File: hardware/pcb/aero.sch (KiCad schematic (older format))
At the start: 0 parts

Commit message: version 1 of layout
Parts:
- added H1: Vreg_Header, Socket_Strips:Socket_Strip_Straight_1x02, symbol Vreg_Header
- added P1: CONN_01X09, Socket_Strips:Socket_Strip_Straight_1x09, symbol CONN_01X09
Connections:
- net nRF8001/ACTIVE: now also P1.9 (P9)
- net nRF8001/MISO: now also P1.3 (P3)
- net nRF8001/MOSI: now also P1.4 (P4)
- net nRF8001/SCK: now also P1.6 (P6)
- net nRF8001/TXD: now also P1.8 (P8)
- net nRF8001/~RDYN: now also P1.2 (P2)
- net nRF8001/~REQN: now also P1.5 (P5)
- net nRF8001/~RESET: now also P1.1 (P1)
- new net nRF8001/Gnd: H1.2 (GND)
- new net nRF8001/RXD: P1.7 (P7)
- new net nRF8001/Vcc: H1.1 (Vcc)
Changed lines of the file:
@@
 LIBS:contrib
 LIBS:valves
+LIBS:aero-cache
 EELAYER 25 0
 EELAYER END
@@
 Comment4 ""
 $EndDescr
+$Comp
+L CONN_01X09 P1
+U 1 1 551C5BBD
+P 7550 1650
+F 0 "P1" H 7550 2150 50  0000 C CNN
+F 1 "CONN_01X09" V 7650 1650 50  0000 C CNN
+F 2 "Socket_Strips:Socket_Strip_Straight_1x09" H 7550 1650 60  0001 C CNN
+F 3 "" H 7550 1650 60  0000 C CNN
+	1    7550 1650
+	-1   0    0    1
+$EndComp
+$Comp
+L Vreg_Header H1
+U 1 1 551C5F7E
+P 7550 2450
+F 0 "H1" H 7500 2400 60  0000 C CNN
+F 1 "Vreg_Header" V 7350 2400 60  0000 C CNN
+F 2 "Socket_Strips:Socket_Strip_Straight_1x02" H 7550 2450 60  0001 C CNN
+F 3 "" H 7550 2450 60  0000 C CNN
+	1    7550 2450
+	1    0    0    -1
+$EndComp
+Wire Wire Line
+	7800 2300 8000 2300
+Wire Wire Line
+	8000 2400 7800 2400
 $Sheet
 S 8000 1150 1950 1350
@@
 F0 "nRF8001" 60
 F1 "nrf8001.sch" 60
-F2 "MOSI" I L 8000 1450 60
-F3 "MISO" O L 8000 1550 60
-F4 "~RDYN" O L 8000 1650 60
-F5 "~REQN" I L 8000 1750 60
-F6 "SCK" I L 8000 1350 60
-F7 "~RESET" I L 8000 1850 60
-F8 "ACTIVE" I L 8000 1950 60
-F9 "TXD" O L 8000 2050 60
+F2 "Vcc" I L 8000 2300 60
+F3 "Gnd" I L 8000 2400 60
+F4 "MOSI" I L 8000 1750 60
+F5 "MISO" O L 8000 1850 60
+F6 "~RDYN" O L 8000 1950 60
+F7 "~REQN" I L 8000 1650 60
+F8 "SCK" I L 8000 1550 60
+F9 "~RESET" I L 8000 2050 60
+F10 "ACTIVE" I L 8000 1250 60
+F11 "TXD" I L 8000 1350 60
+F12 "RXD" I L 8000 1450 60
 $EndSheet
+Wire Wire Line
+	7750 1250 8000 1250
+Wire Wire Line
+	8000 1350 7750 1350
+Wire Wire Line
+	7750 1450 8000 1450
+Wire Wire Line
+	8000 1550 7750 1550
+Wire Wire Line
+	8000 1650 7750 1650
+Wire Wire Line
+	7750 1750 8000 1750
+Wire Wire Line
+	8000 1850 7750 1850
+Wire Wire Line
+	7750 1950 8000 1950
+Wire Wire Line
+	8000 2050 7750 2050
 $EndSCHEMATC

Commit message: pcb updates
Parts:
- added P1: CONN_01X02, Pin_Headers:Pin_Header_Straight_1x02, symbol CONN_01X02
- H1: footprint Socket_Strips:Socket_Strip_Straight_1x02 -> Pin_Headers:Pin_Header_Straight_1x02
- P2: renamed from P1; footprint Socket_Strips:Socket_Strip_Straight_1x09 -> Pin_Headers:Pin_Header_Straight_1x09
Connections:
- net labels added: GND, VCC
- wire segments 11 -> 16
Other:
- moved on the sheet: H1
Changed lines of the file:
@@
 $Descr A4 11693 8268
 encoding utf-8
-Sheet 1 2
+Sheet 1 3
 Title ""
 Date ""
@@
 $EndDescr
 $Comp
-L CONN_01X09 P1
+L CONN_01X09 P2
 U 1 1 551C5BBD
 P 7550 1650
-F 0 "P1" H 7550 2150 50  0000 C CNN
+F 0 "P2" H 7550 2150 50  0000 C CNN
 F 1 "CONN_01X09" V 7650 1650 50  0000 C CNN
-F 2 "Socket_Strips:Socket_Strip_Straight_1x09" H 7550 1650 60  0001 C CNN
+F 2 "Pin_Headers:Pin_Header_Straight_1x09" H 7550 1650 60  0001 C CNN
 F 3 "" H 7550 1650 60  0000 C CNN
 	1    7550 1650
@@
 L Vreg_Header H1
 U 1 1 551C5F7E
-P 7550 2450
-F 0 "H1" H 7500 2400 60  0000 C CNN
-F 1 "Vreg_Header" V 7350 2400 60  0000 C CNN
-F 2 "Socket_Strips:Socket_Strip_Straight_1x02" H 7550 2450 60  0001 C CNN
-F 3 "" H 7550 2450 60  0000 C CNN
-	1    7550 2450
+P 6000 3250
+F 0 "H1" H 5950 3200 60  0000 C CNN
+F 1 "Vreg_Header" V 5800 3200 60  0000 C CNN
+F 2 "Pin_Headers:Pin_Header_Straight_1x02" H 6000 3250 60  0001 C CNN
+F 3 "" H 6000 3250 60  0000 C CNN
+	1    6000 3250
 	1    0    0    -1
 $EndComp
-Wire Wire Line
-	7800 2300 8000 2300
-Wire Wire Line
-	8000 2400 7800 2400
 $Sheet
 S 8000 1150 1950 1350
@@
 F0 "nRF8001" 60
 F1 "nrf8001.sch" 60
-F2 "Vcc" I L 8000 2300 60
-F3 "Gnd" I L 8000 2400 60
-F4 "MOSI" I L 8000 1750 60
-F5 "MISO" O L 8000 1850 60
-F6 "~RDYN" O L 8000 1950 60
-F7 "~REQN" I L 8000 1650 60
-F8 "SCK" I L 8000 1550 60
-F9 "~RESET" I L 8000 2050 60
-F10 "ACTIVE" I L 8000 1250 60
-F11 "TXD" I L 8000 1350 60
-F12 "RXD" I L 8000 1450 60
+F2 "MOSI" I L 8000 1750 60
+F3 "MISO" O L 8000 1850 60
+F4 "~RDYN" O L 8000 1950 60
+F5 "~REQN" I L 8000 1650 60
+F6 "SCK" I L 8000 1550 60
+F7 "~RESET" I L 8000 2050 60
+F8 "ACTIVE" I L 8000 1250 60
+F9 "TXD" I L 8000 1350 60
+F10 "RXD" I L 8000 1450 60
 $EndSheet
+$Sheet
+S 2800 1050 1400 1200
+U 551EEA41
+F0 "sensors" 60
+F1 "sensors.sch" 60
+F2 "SDA" I R 4200 1250 60
+F3 "SCLK" I R 4200 1400 60
+$EndSheet
+Text GLabel 6900 3050 2    60   Input ~ 0
+VCC
+Text GLabel 6900 3250 2    60   Input ~ 0
+GND
+$Comp
+L CONN_01X02 P1
+U 1 1 551EFD46
+P 4700 1300
+F 0 "P1" H 4700 1450 50  0000 C CNN
+F 1 "CONN_01X02" V 4800 1300 50  0000 C CNN
+F 2 "Pin_Headers:Pin_Header_Straight_1x02" H 4700 1300 60  0001 C CNN
+F 3 "" H 4700 1300 60  0000 C CNN
+	1    4700 1300
+	1    0    0    -1
+$EndComp
 Wire Wire Line
 	7750 1250 8000 1250
@@
 Wire Wire Line
 	8000 2050 7750 2050
+Wire Wire Line
+	6900 3250 6250 3250
+Wire Wire Line
+	6250 3250 6250 3200
+Wire Wire Line
+	6250 3100 6900 3100
+Wire Wire Line
+	6900 3100 6900 3050
+Wire Wire Line
+	4200 1250 4500 1250
+Wire Wire Line
+	4200 1400 4500 1400
+Wire Wire Line
+	4500 1400 4500 1350
 $EndSCHEMATC

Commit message: PCB updates, new docs, file reorg
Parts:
- removed P1: CONN_01X02, Pin_Headers:Pin_Header_Straight_1x02, symbol CONN_01X02
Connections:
- wire segments 16 -> 13
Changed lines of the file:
@@
 $Descr A4 11693 8268
 encoding utf-8
-Sheet 1 3
+Sheet 1 4
 Title ""
 Date ""
@@
 $EndSheet
 $Sheet
-S 2800 1050 1400 1200
+S 2800 1050 700  650
 U 551EEA41
-F0 "sensors" 60
-F1 "sensors.sch" 60
-F2 "SDA" I R 4200 1250 60
-F3 "SCLK" I R 4200 1400 60
+F0 "ms5611" 60
+F1 "ms5611.sch" 60
+F2 "EN" I R 3500 1350 60
+F3 "SCLK" I R 3500 1650 60
+F4 "MOSI" I R 3500 1450 60
+F5 "MISO" I R 3500 1550 60
 $EndSheet
 Text GLabel 6900 3050 2    60   Input ~ 0
@@
 Text GLabel 6900 3250 2    60   Input ~ 0
 GND
-$Comp
-L CONN_01X02 P1
-U 1 1 551EFD46
-P 4700 1300
-F 0 "P1" H 4700 1450 50  0000 C CNN
-F 1 "CONN_01X02" V 4800 1300 50  0000 C CNN
-F 2 "Pin_Headers:Pin_Header_Straight_1x02" H 4700 1300 60  0001 C CNN
-F 3 "" H 4700 1300 60  0000 C CNN
-	1    4700 1300
-	1    0    0    -1
-$EndComp
 Wire Wire Line
 	7750 1250 8000 1250
@@
 Wire Wire Line
 	6900 3100 6900 3050
-Wire Wire Line
-	4200 1250 4500 1250
-Wire Wire Line
-	4200 1400 4500 1400
-Wire Wire Line
-	4500 1400 4500 1350
+$Sheet
+S 2600 2450 650  500
+U 5527E8E0
+F0 "bmx055" 60
+F1 "bmx055.sch" 60
+$EndSheet
 $EndSCHEMATC

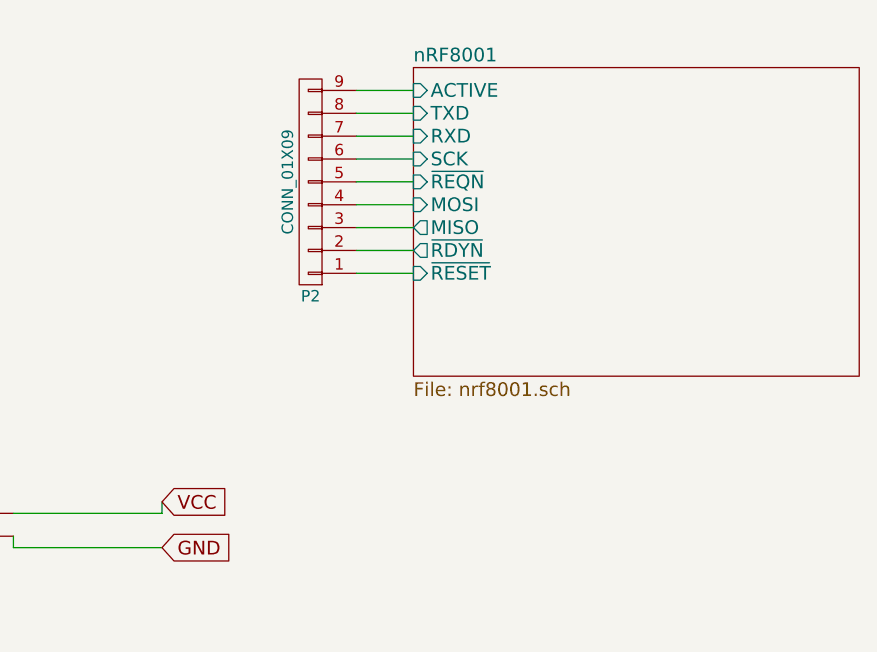
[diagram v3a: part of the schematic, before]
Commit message: Removed nRF8001 connections; beginning eventual design
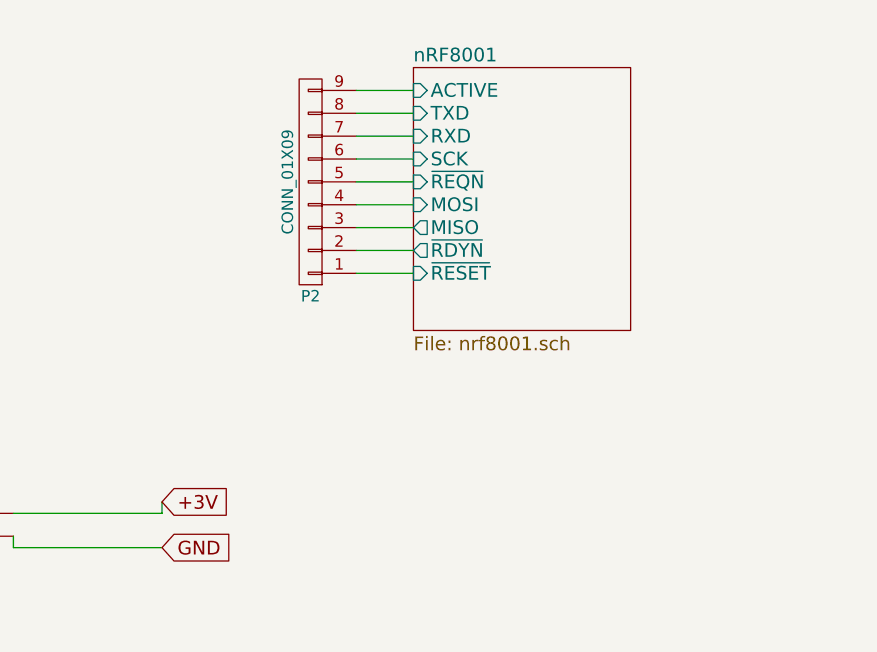
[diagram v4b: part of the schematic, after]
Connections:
- net VCC renamed +3V
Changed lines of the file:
@@
 $EndComp
 $Sheet
-S 8000 1150 1950 1350
+S 8000 1150 950  1150
 U 551C09E8
 F0 "nRF8001" 60
@@
 $EndSheet
 Text GLabel 6900 3050 2    60   Input ~ 0
-VCC
++3V
 Text GLabel 6900 3250 2    60   Input ~ 0
 GND

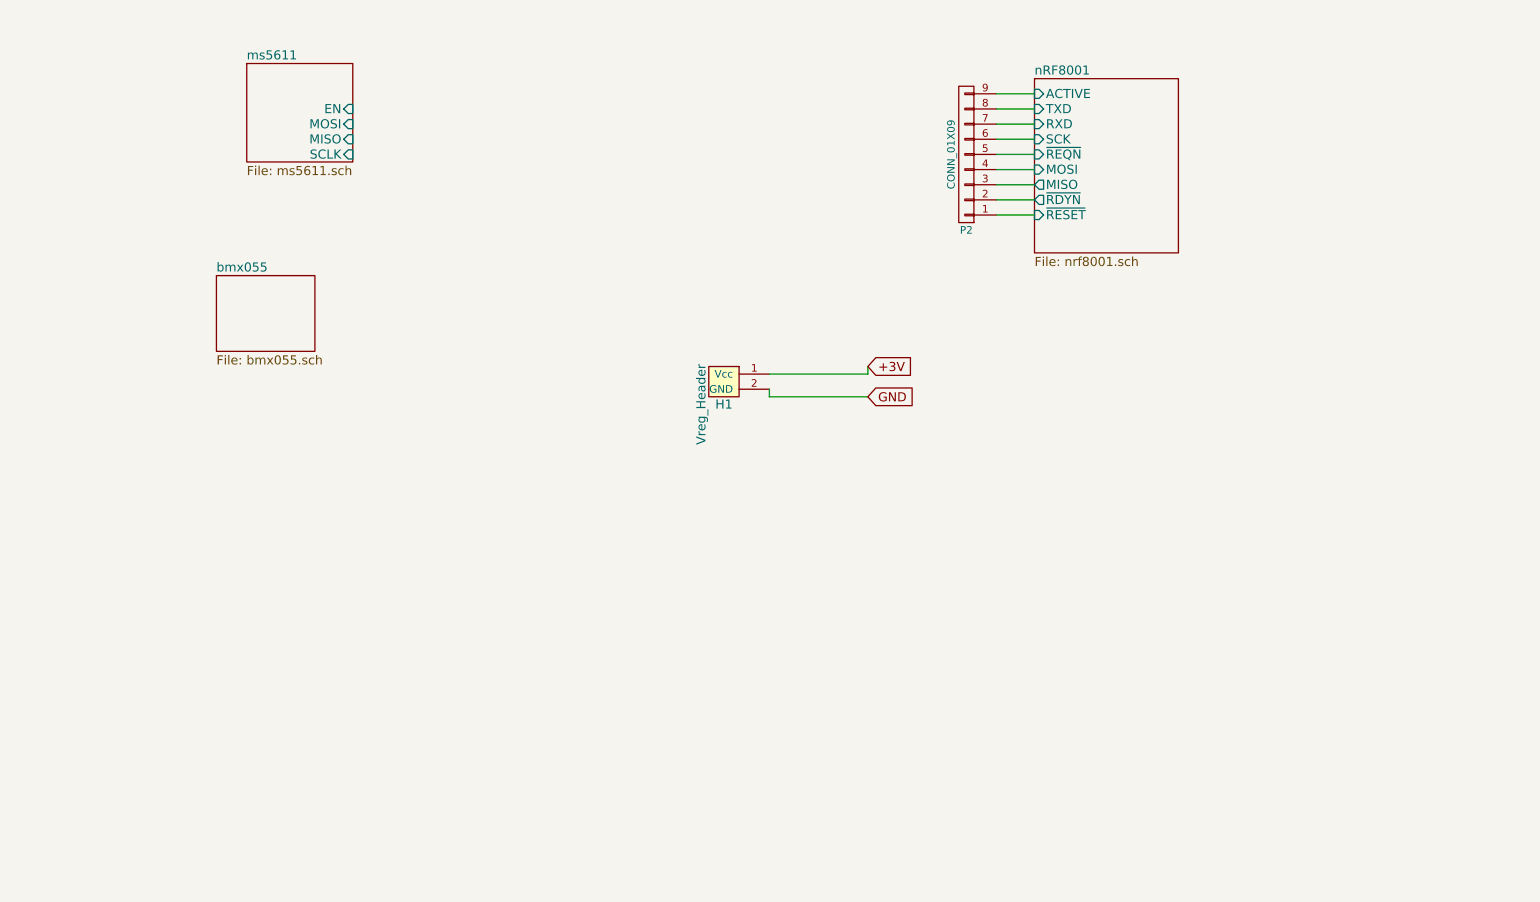
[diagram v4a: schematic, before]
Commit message: Added mcu, connected nrf8001 and flash, new footprint, other changes
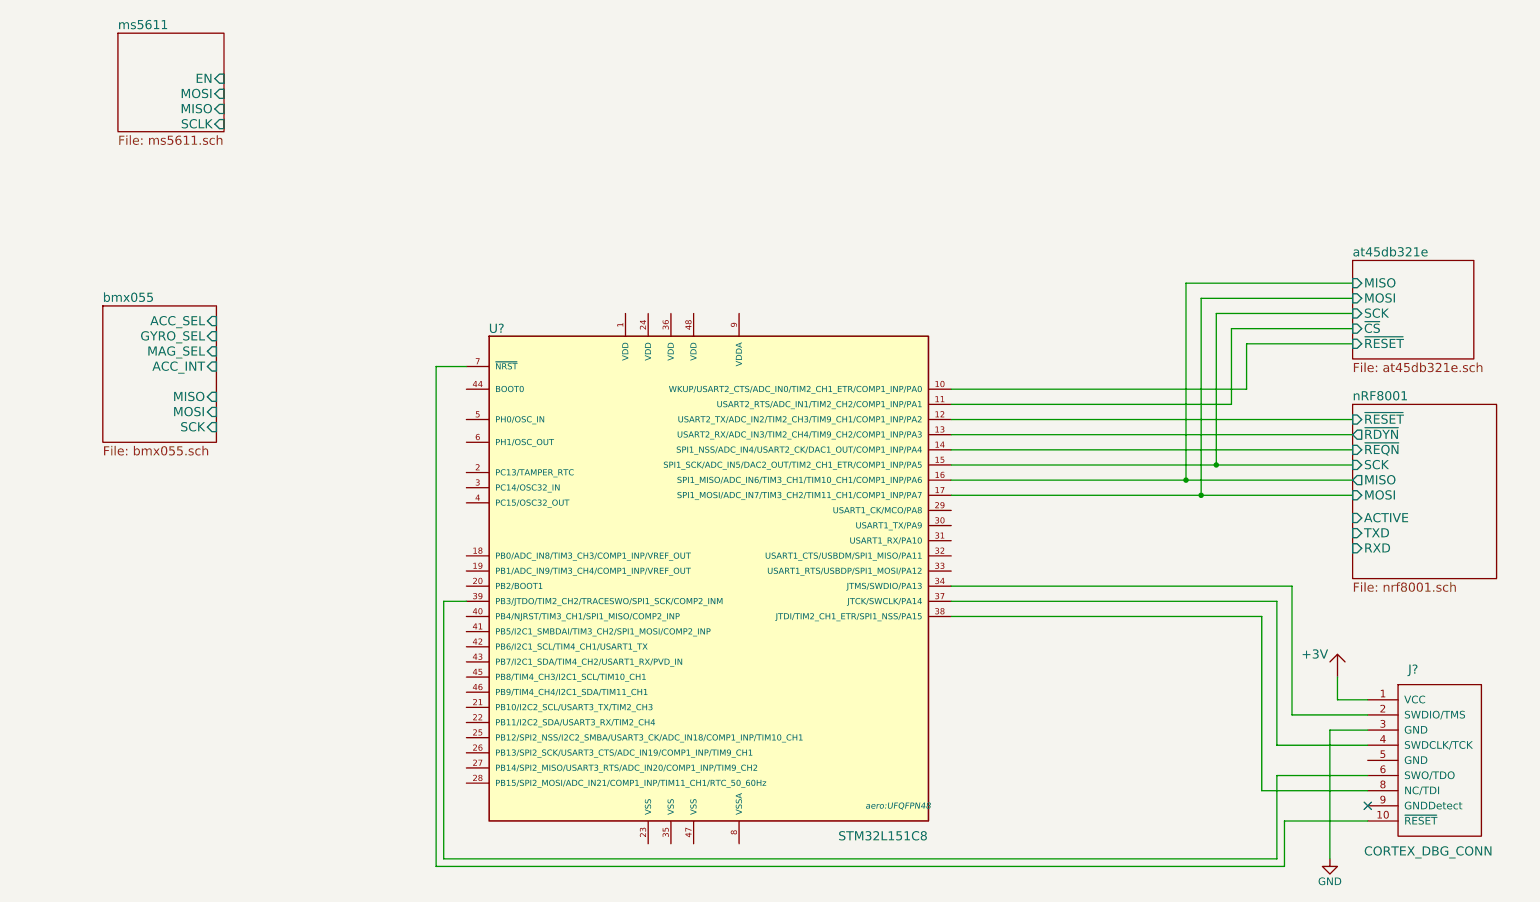
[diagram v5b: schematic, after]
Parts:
- removed H1: Vreg_Header, Pin_Headers:Pin_Header_Straight_1x02, symbol Vreg_Header
- removed P2: CONN_01X09, Pin_Headers:Pin_Header_Straight_1x09, symbol CONN_01X09
- added J?: CORTEX_DBG_CONN, symbol CORTEX_DBG_CONN
- added U?: STM32L151C8, aero:UFQFPN48, symbol STM32L151C8
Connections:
- net GND: now also J?.3 (GND)
- net nRF8001/~RDYN: now also U?.13 (USART2_RX/ADC_IN3/TIM2_CH4/TIM9_CH2/COMP1_INP/PA3)
- net nRF8001/~REQN: now also U?.14 (SPI1_NSS/ADC_IN4/USART2_CK/DAC1_OUT/COMP1_INP/PA4)
- net nRF8001/~RESET: now also U?.12 (USART2_TX/ADC_IN2/TIM2_CH3/TIM9_CH1/COMP1_INP/PA2)
- new net: J?.2 (SWDIO/TMS), U?.34 (JTMS/SWDIO/PA13)
- new net: J?.4 (SWDCLK/TCK), U?.37 (JTCK/SWCLK/PA14)
- new net: J?.8 (NC/TDI), U?.38 (JTDI/TIM2_CH1_ETR/SPI1_NSS/PA15)
- new net: J?.6 (SWO/TDO), U?.39 (PB3/JTDO/TIM2_CH2/TRACESWO/SPI1_SCK/COMP2_INM)
- new net: J?.10 (~RESET), U?.7 (~NRST)
- new net +3V3: J?.1 (VCC)
- new net at45db321e/MISO: U?.16 (SPI1_MISO/ADC_IN6/TIM3_CH1/TIM10_CH1/COMP1_INP/PA6)
- new net at45db321e/MOSI: U?.17 (SPI1_MOSI/ADC_IN7/TIM3_CH2/TIM11_CH1/COMP1_INP/PA7)
- new net at45db321e/SCK: U?.15 (SPI1_SCK/ADC_IN5/DAC2_OUT/TIM2_CH1_ETR/COMP1_INP/PA5)
- new net at45db321e/~CS: U?.11 (USART2_RTS/ADC_IN1/TIM2_CH2/COMP1_INP/PA1)
- new net at45db321e/~RESET: U?.10 (WKUP/USART2_CTS/ADC_IN0/TIM2_CH1_ETR/COMP1_INP/PA0)
- no-connect marks 0 -> 1
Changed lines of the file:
@@
 $Descr A4 11693 8268
 encoding utf-8
-Sheet 1 4
+Sheet 1 5
 Title ""
 Date ""
@@
 Comment4 ""
 $EndDescr
-$Comp
-L CONN_01X09 P2
-U 1 1 551C5BBD
-P 7550 1650
-F 0 "P2" H 7550 2150 50  0000 C CNN
-F 1 "CONN_01X09" V 7650 1650 50  0000 C CNN
-F 2 "Pin_Headers:Pin_Header_Straight_1x09" H 7550 1650 60  0001 C CNN
-F 3 "" H 7550 1650 60  0000 C CNN
-	1    7550 1650
-	-1   0    0    1
-$EndComp
-$Comp
-L Vreg_Header H1
-U 1 1 551C5F7E
-P 6000 3250
-F 0 "H1" H 5950 3200 60  0000 C CNN
-F 1 "Vreg_Header" V 5800 3200 60  0000 C CNN
-F 2 "Pin_Headers:Pin_Header_Straight_1x02" H 6000 3250 60  0001 C CNN
-F 3 "" H 6000 3250 60  0000 C CNN
-	1    6000 3250
-	1    0    0    -1
-$EndComp
 $Sheet
-S 8000 1150 950  1150
+S 10100 3300 950  1150
 U 551C09E8
 F0 "nRF8001" 60
 F1 "nrf8001.sch" 60
-F2 "MOSI" I L 8000 1750 60
-F3 "MISO" O L 8000 1850 60
-F4 "~RDYN" O L 8000 1950 60
-F5 "~REQN" I L 8000 1650 60
-F6 "SCK" I L 8000 1550 60
-F7 "~RESET" I L 8000 2050 60
-F8 "ACTIVE" I L 8000 1250 60
-F9 "TXD" I L 8000 1350 60
-F10 "RXD" I L 8000 1450 60
+F2 "MOSI" I L 10100 3900 60
+F3 "MISO" O L 10100 3800 60
+F4 "~RDYN" O L 10100 3500 60
+F5 "~REQN" I L 10100 3600 60
+F6 "SCK" I L 10100 3700 60
+F7 "~RESET" I L 10100 3400 60
+F8 "ACTIVE" I L 10100 4050 60
+F9 "TXD" I L 10100 4150 60
+F10 "RXD" I L 10100 4250 60
 $EndSheet
 $Sheet
-S 2800 1050 700  650
+S 1950 850  700  650
 U 551EEA41
 F0 "ms5611" 60
 F1 "ms5611.sch" 60
-F2 "EN" I R 3500 1350 60
-F3 "SCLK" I R 3500 1650 60
-F4 "MOSI" I R 3500 1450 60
-F5 "MISO" I R 3500 1550 60
+F2 "EN" I R 2650 1150 60
+F3 "SCLK" I R 2650 1450 60
+F4 "MOSI" I R 2650 1250 60
+F5 "MISO" I R 2650 1350 60
 $EndSheet
-Text GLabel 6900 3050 2    60   Input ~ 0
-+3V
-Text GLabel 6900 3250 2    60   Input ~ 0
-GND
-Wire Wire Line
-	7750 1250 8000 1250
-Wire Wire Line
-	8000 1350 7750 1350
-Wire Wire Line
-	7750 1450 8000 1450
-Wire Wire Line
-	8000 1550 7750 1550
-Wire Wire Line
-	8000 1650 7750 1650
-Wire Wire Line
-	7750 1750 8000 1750
-Wire Wire Line
-	8000 1850 7750 1850
-Wire Wire Line
-	7750 1950 8000 1950
-Wire Wire Line
-	8000 2050 7750 2050
-Wire Wire Line
-	6900 3250 6250 3250
-Wire Wire Line
-	6250 3250 6250 3200
-Wire Wire Line
-	6250 3100 6900 3100
-Wire Wire Line
-	6900 3100 6900 3050
 $Sheet
-S 2600 2450 650  500
+S 1850 2650 750  900
 U 5527E8E0
 F0 "bmx055" 60
 F1 "bmx055.sch" 60
+F2 "ACC_SEL" I R 2600 2750 60
+F3 "GYRO_SEL" I R 2600 2850 60
+F4 "MAG_SEL" I R 2600 2950 60
+F5 "ACC_INT" I R 2600 3050 60
+F6 "MISO" I R 2600 3250 60
+F7 "MOSI" I R 2600 3350 60
+F8 "SCK" I R 2600 3450 60
 $EndSheet
+$Comp
+L STM32L151C8 U?
+U 1 1 552EE402
+P 5750 4450
+F 0 "U?" H 4450 6100 60  0000 C CNN
+F 1 "STM32L151C8" H 7000 2750 60  0000 C CNN
+F 2 "aero:UFQFPN48" H 7100 2950 40  0000 C CIN
+F 3 "" H 5750 4450 60  0000 C CNN
+	1    5750 4450
+	1    0    0    -1
+$EndComp
+$Comp
+L CORTEX_DBG_CONN J?
+U 1 1 552F1C1E
+P 10500 5550
+F 0 "J?" H 10500 6050 60  0000 C CNN
+F 1 "CORTEX_DBG_CONN" H 10600 4850 60  0000 C CNN
+F 2 "" H 10350 5550 60  0000 C CNN
+F 3 "" H 10350 5550 60  0000 C CNN
+	1    10500 5550
+	1    0    0    -1
+$EndComp
+$Comp
+L +3V #PWR?
+U 1 1 552F1D3F
+P 10000 5100
+F 0 "#PWR?" H 10000 5000 60  0001 C CNN
+F 1 "+3V" H 9850 5250 60  0000 C CNN
+F 2 "" H 10000 5100 60  0000 C CNN
+F 3 "" H 10000 5100 60  0000 C CNN
+	1    10000 5100
+	1    0    0    -1
+$EndComp
+$Comp
+L GND #PWR?
+U 1 1 552F1F7F
+P 9950 6300
+F 0 "#PWR?" H 9950 6050 50  0001 C CNN
+F 1 "GND" H 9950 6150 50  0000 C CNN
+F 2 "" H 9950 6300 60  0000 C CNN
+F 3 "" H 9950 6300 60  0000 C CNN
+	1    9950 6300
+	1    0    0    -1
+$EndComp
+NoConn ~ 10200 5950
+$Sheet
+S 10100 2350 800  650
+U 552F3B87
+F0 "at45db321e" 60
+F1 "at45db321e.sch" 60
+F2 "MOSI" I L 10100 2600 60
+F3 "MISO" I L 10100 2500 60
+F4 "SCK" I L 10100 2700 60
+F5 "~CS" I L 10100 2800 60
+F6 "~RESET" I L 10100 2900 60
+$EndSheet
+Wire Wire Line
+	10100 3900 7450 3900
+Wire Wire Line
+	7450 3700 10100 3700
+Wire Wire Line
+	10100 3800 7450 3800
+Wire Wire Line
+	7450 3600 10100 3600
+Wire Wire Line
+	10100 3500 7450 3500
+Wire Wire Line
+	7450 3400 10100 3400
+Wire Wire Line
+	10200 5250 10000 5250
+Wire Wire Line
+	10000 5250 10000 5100
+Wire Wire Line
+	10200 5350 9700 5350
+Wire Wire Line
+	9700 5350 9700 4500
+Wire Wire Line
+	9700 4500 7450 4500
+Wire Wire Line
+	7450 4600 9600 4600
+Wire Wire Line
+	9600 4600 9600 5550
+Wire Wire Line
+	9600 5550 10200 5550
+Wire Wire Line
+	4250 4600 4100 4600
+Wire Wire Line
+	4100 4600 4100 6300
+Wire Wire Line
+	4100 6300 9600 6300
+Wire Wire Line
+	9600 6300 9600 5750
+Wire Wire Line
+	9600 5750 10200 5750
+Wire Wire Line
+	7450 4700 9500 4700
+Wire Wire Line
+	9500 4700 9500 5850
+Wire Wire Line
+	9500 5850 10200 5850
+Wire Wire Line
+	10200 5450 9950 5450
+Wire Wire Line
+	9950 5450 9950 6300
+Wire Wire Line
+	10100 2500 9000 2500
+Wire Wire Line
+	9000 2500 9000 3800
+Connection ~ 9000 3800
+Wire Wire Line
+	10100 2700 9200 2700
+Wire Wire Line
+	9200 2700 9200 3700
+Connection ~ 9200 3700
+Wire Wire Line
+	10100 2800 9300 2800
+Wire Wire Line
+	9300 2800 9300 3300
+Wire Wire Line
+	9300 3300 7450 3300
+Wire Wire Line
+	10100 2900 9400 2900
+Wire Wire Line
+	9400 2900 9400 3200
+Wire Wire Line
+	9400 3200 7450 3200
+Wire Wire Line
+	10200 6050 9650 6050
+Wire Wire Line
+	9650 6050 9650 6350
+Wire Wire Line
+	9650 6350 4050 6350
+Wire Wire Line
+	4050 6350 4050 3050
+Wire Wire Line
+	4050 3050 4250 3050
+Wire Wire Line
+	10100 2600 9100 2600
+Wire Wire Line
+	9100 2600 9100 3900
+Connection ~ 9100 3900
 $EndSCHEMATC
